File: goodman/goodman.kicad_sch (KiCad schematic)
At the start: 10 parts, among them J1 TSM-110-01-T-DV, J2 09561527613, Q1 BSS138BKT116

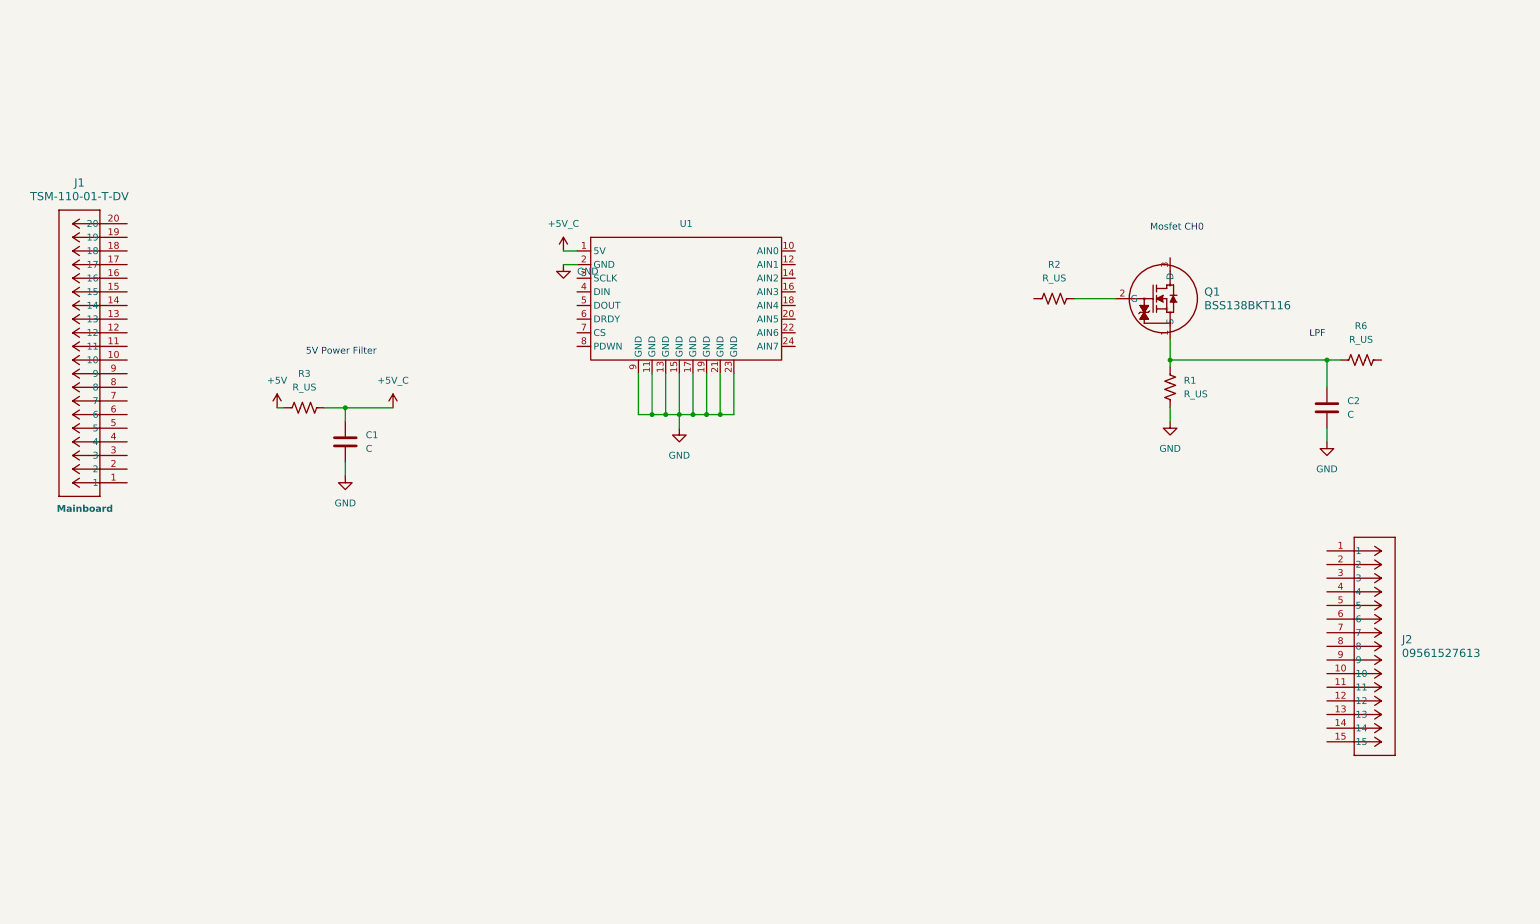
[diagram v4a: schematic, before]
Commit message: Added signal net names.
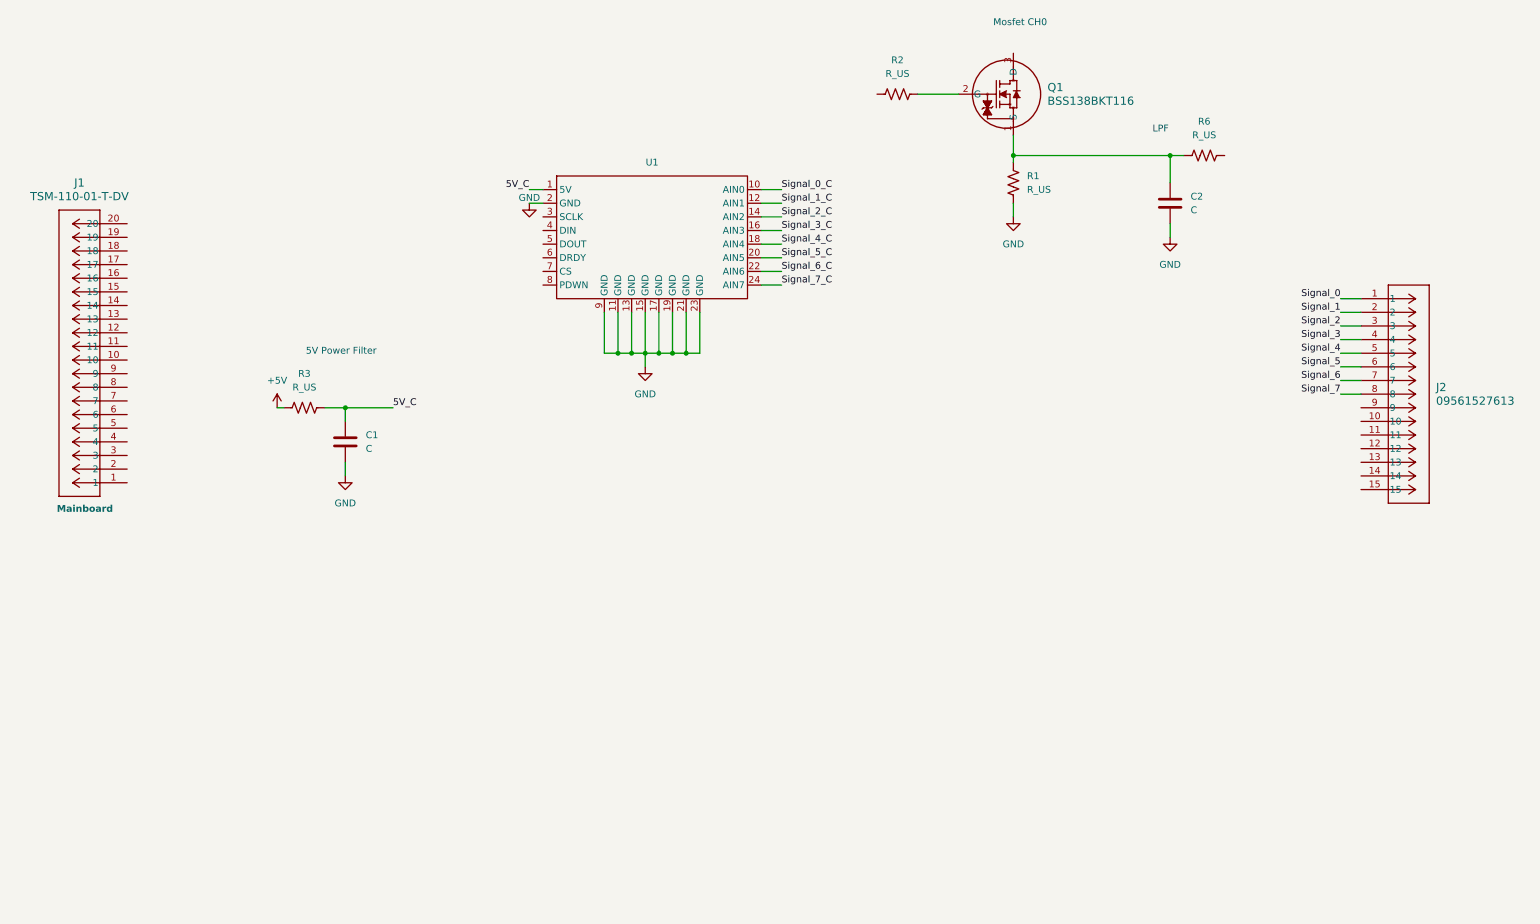
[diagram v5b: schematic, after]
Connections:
- net Signal_0_C: now reaches U1.10 (AIN0)
- net Signal_1_C: now reaches U1.12 (AIN1)
- net Signal_2_C: now reaches U1.14 (AIN2)
- net Signal_3_C: now reaches U1.16 (AIN3)
- net Signal_4_C: now reaches U1.18 (AIN4)
- net Signal_5_C: now reaches U1.20 (AIN5)
- net Signal_6_C: now reaches U1.22 (AIN6)
- net Signal_7_C: now reaches U1.24 (AIN7)
- net Signal_0: now reaches J2.1
- net Signal_1: now reaches J2.2
- net Signal_2: now reaches J2.3
- net Signal_3: now reaches J2.4
- net Signal_4: now reaches J2.5
- net Signal_5: now reaches J2.6
- net Signal_6: now reaches J2.7
- net Signal_7: now reaches J2.8
- net +5V_C renamed 5V_C
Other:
- moved on the sheet: C2, J2, Q1, R1, R2, R6, U1

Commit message: Added sheet hierarchy with mosfet logic and added netnames for connections.
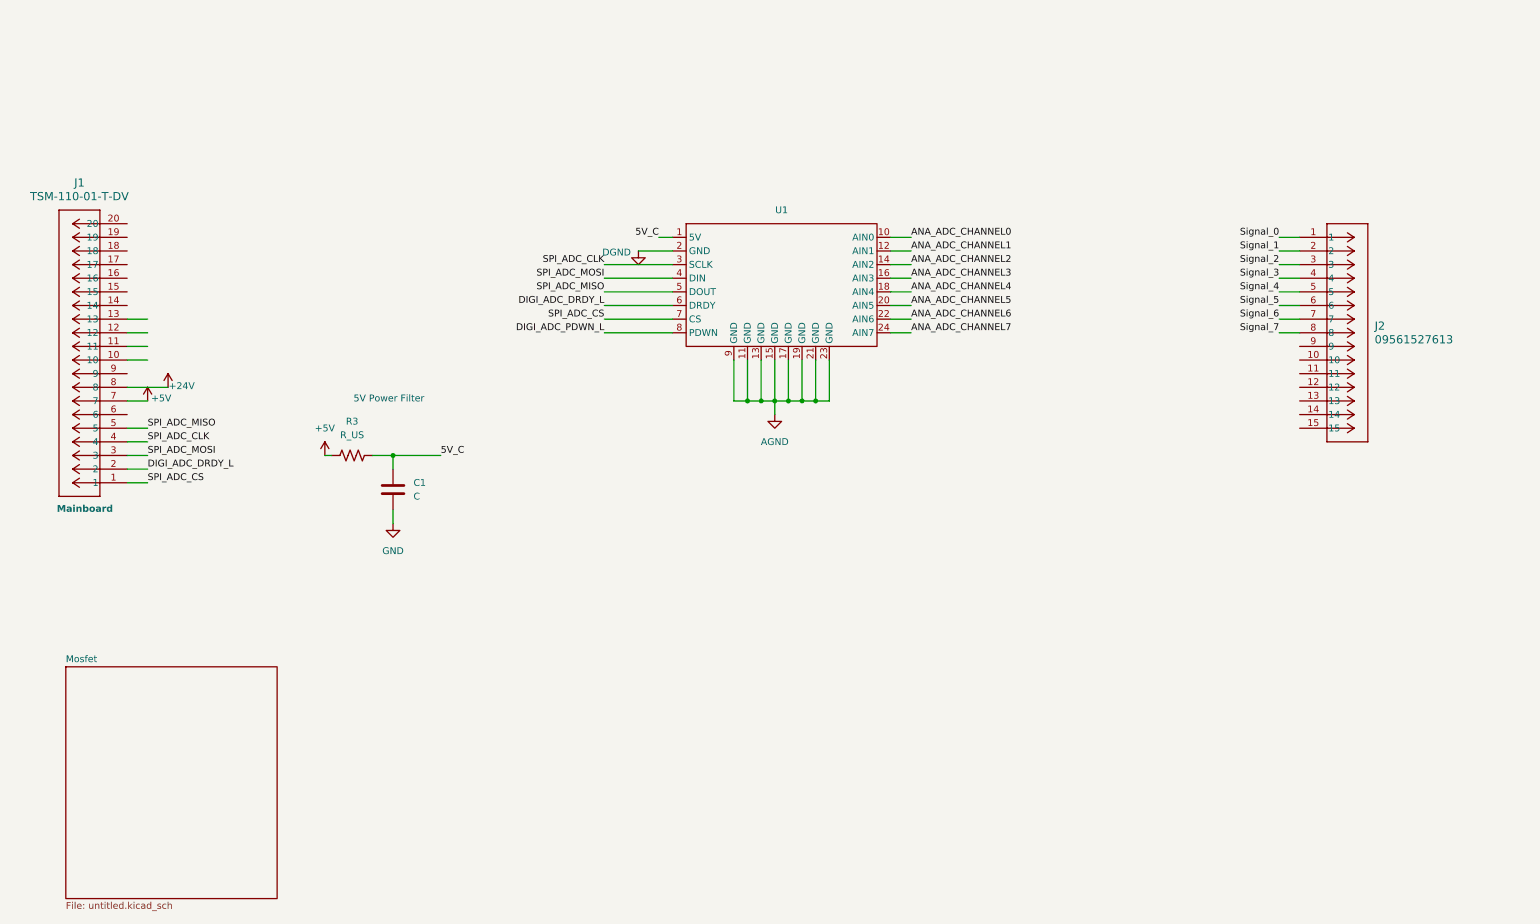
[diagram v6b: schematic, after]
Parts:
- removed C2: C, symbol Device:C
- removed Q1: BSS138BKT116, SOT23_BSS138_ROM, symbol Goodman Local:BSS138BKT116
- removed R1, R2, R6: R_US, symbol Device:R_US
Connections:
- net +5V: now also J1.7
- net GND: no longer U1.11 (GND), U1.13 (GND), U1.15 (GND), U1.17 (GND), U1.19 (GND), U1.2 (GND), U1.21 (GND), U1.23 (GND), U1.9 (GND)
- net SPI_ADC_CLK: now reaches U1.3 (SCLK)
- net SPI_ADC_CLK: now also J1.4
- net SPI_ADC_MOSI: now reaches U1.4 (DIN)
- net SPI_ADC_MOSI: now also J1.3
- net SPI_ADC_MISO: now reaches U1.5 (DOUT)
- net SPI_ADC_MISO: now also J1.5
- net DIGI_ADC_DRDY_L: now reaches U1.6 (DRDY)
- net DIGI_ADC_DRDY_L: now also J1.2
- net SPI_ADC_CS: now reaches U1.7 (CS)
- net SPI_ADC_CS: now also J1.1
- net DIGI_ADC_PDWN_L: now reaches U1.8 (PDWN)
- net +24V: now reaches J1.8
- net Signal_0_C renamed ANA_ADC_CHANNEL0
- net Signal_1_C renamed ANA_ADC_CHANNEL1
- net Signal_2_C renamed ANA_ADC_CHANNEL2
- net Signal_3_C renamed ANA_ADC_CHANNEL3
- net Signal_4_C renamed ANA_ADC_CHANNEL4
- net Signal_5_C renamed ANA_ADC_CHANNEL5
- net Signal_6_C renamed ANA_ADC_CHANNEL6
- net Signal_7_C renamed ANA_ADC_CHANNEL7
- new net AGND: U1.11 (GND), U1.13 (GND), U1.15 (GND), U1.17 (GND), U1.19 (GND), U1.21 (GND), U1.23 (GND), U1.9 (GND)
- new net DGND: U1.2 (GND)
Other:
- added sheet Mosfet (untitled.kicad_sch)
- note removed: "LPF"
- note removed: "Mosfet CH0"
- moved on the sheet: C1, J2, R3, U1

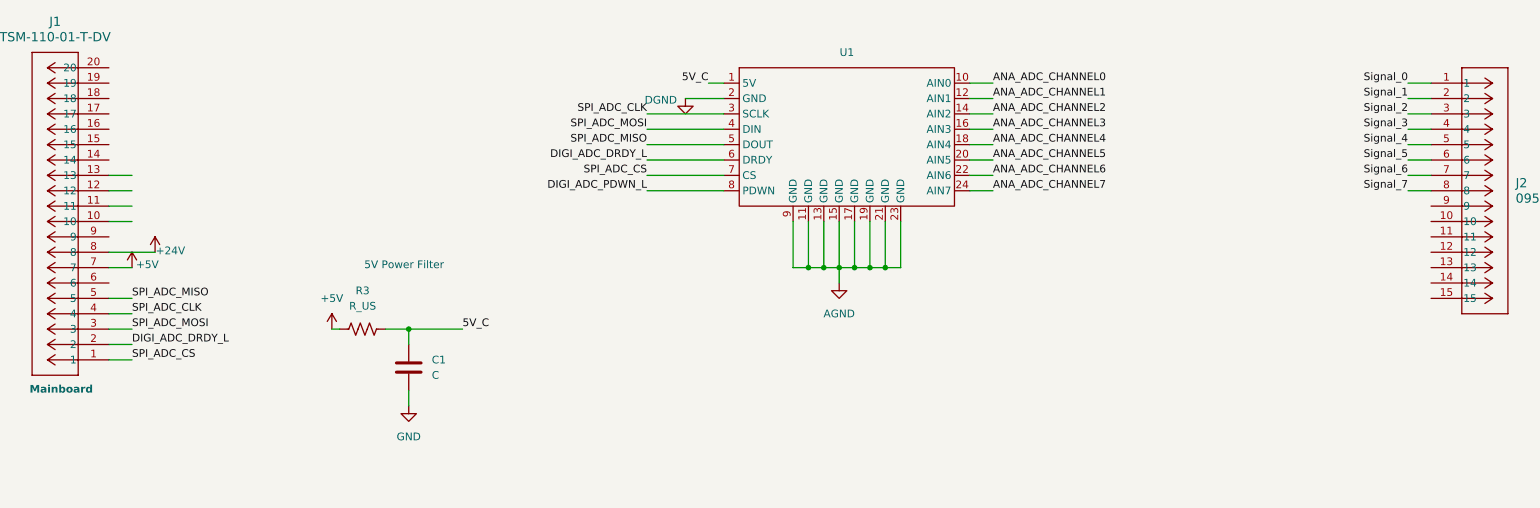
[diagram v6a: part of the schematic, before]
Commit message: Corrected connection net names and mosfet input names.
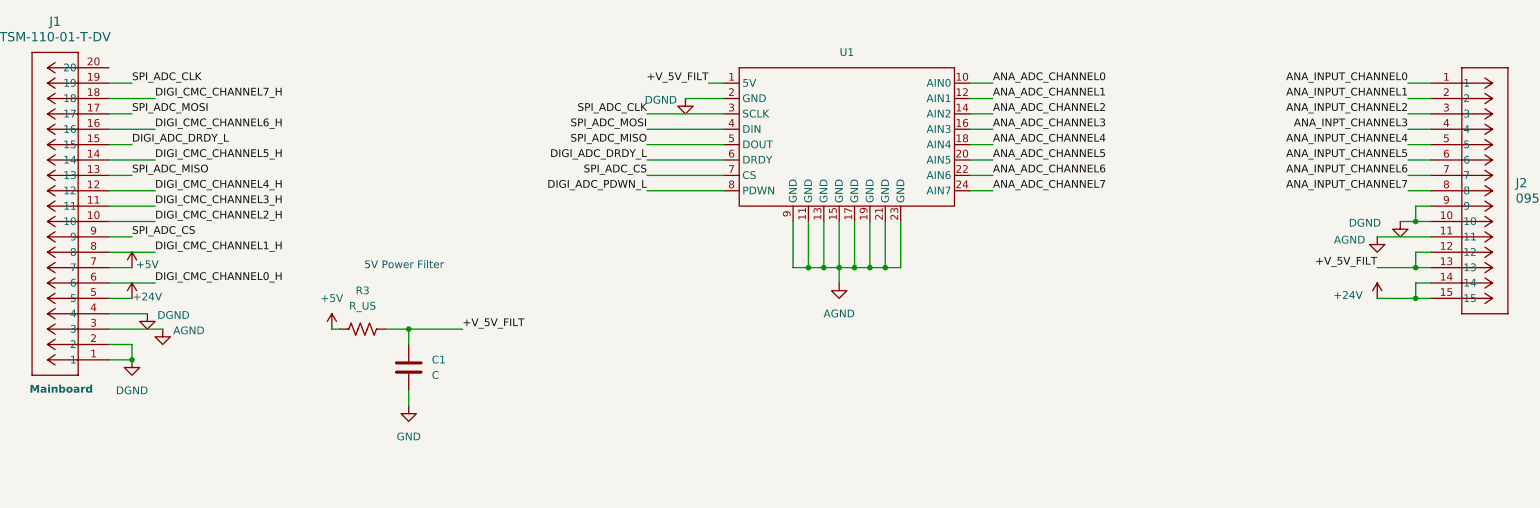
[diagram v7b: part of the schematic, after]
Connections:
- net 5V_C is gone; now on net +V_5V_FILT: C1.1, R3.2, U1.1 (5V)
- net +24V: now also J1.5, J2.14, J2.15; no longer J1.8
- net AGND: now also J1.3, J2.11
- net DGND: now also J1.1, J1.2, J1.4, J2.10, J2.9
- net DIGI_ADC_DRDY_L: now also J1.15; no longer J1.2
- net SPI_ADC_CLK: now also J1.19; no longer J1.4
- net SPI_ADC_CS: now also J1.9; no longer J1.1
- net SPI_ADC_MISO: now also J1.13; no longer J1.5
- net SPI_ADC_MOSI: now also J1.17; no longer J1.3
- net +V_5V_FILT: now reaches J2.12
- net +V_5V_FILT: now also J2.13
- net DIGI_CMC_CHANNEL2_H: now reaches J1.10
- net DIGI_CMC_CHANNEL3_H: now reaches J1.11
- net DIGI_CMC_CHANNEL4_H: now reaches J1.12
- net DIGI_CMC_CHANNEL5_H: now reaches J1.14
- net DIGI_CMC_CHANNEL6_H: now reaches J1.16
- net DIGI_CMC_CHANNEL7_H: now reaches J1.18
- net DIGI_CMC_CHANNEL0_H: now reaches J1.6
- net Signal_0 renamed ANA_INPUT_CHANNEL0
- net Signal_1 renamed ANA_INPUT_CHANNEL1
- net Signal_2 renamed ANA_INPUT_CHANNEL2
- net Signal_3 renamed ANA_INPT_CHANNEL3
- net Signal_4 renamed ANA_INPUT_CHANNEL4
- net Signal_5 renamed ANA_INPUT_CHANNEL5
- net Signal_6 renamed ANA_INPUT_CHANNEL6
- net Signal_7 renamed ANA_INPUT_CHANNEL7
- new net DIGI_CMC_CHANNEL1_H: J1.8
